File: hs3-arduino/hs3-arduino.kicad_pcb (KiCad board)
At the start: 2 copper layers, 68.6 x 53.3 mm, 30 parts, among them J1 Conn_01x02, J1 Serial, J2 USB_C_Receptacle_USB2.0, J4 LED Data, J5 I2C Header, J6 I2C Header, J7 I2C Header, J8 I2C Header, P1 Power, P2 Analog, P3 Digital, P4 Digital, P5 CONN_01X01, P6 CONN_01X01, P7 CONN_01X01, P8 CONN_01X01, SW1 Reset, SW2 Boot Option, U1 AMS1117-3.3, U2 ESP32-WROOM-32E, U3 TXB0102DCT

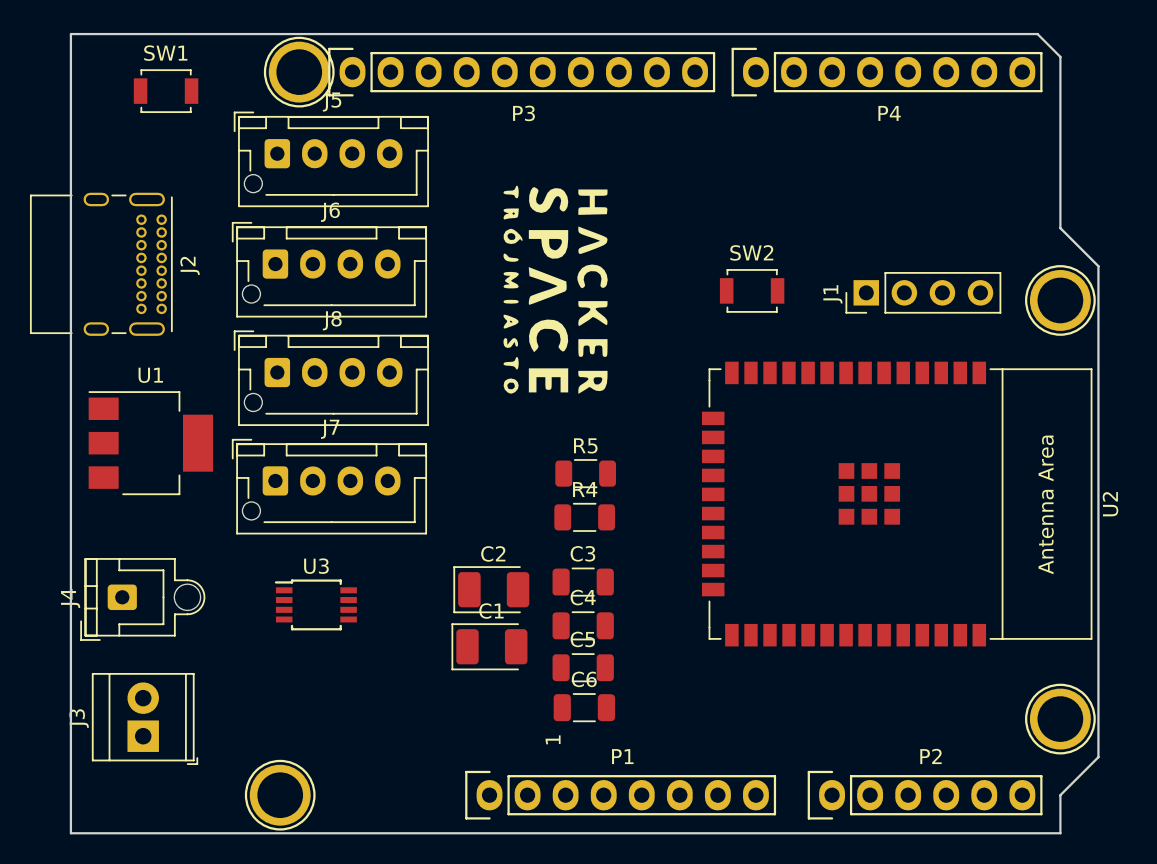
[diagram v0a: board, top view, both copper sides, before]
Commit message: Adding duplicated Arduino pins
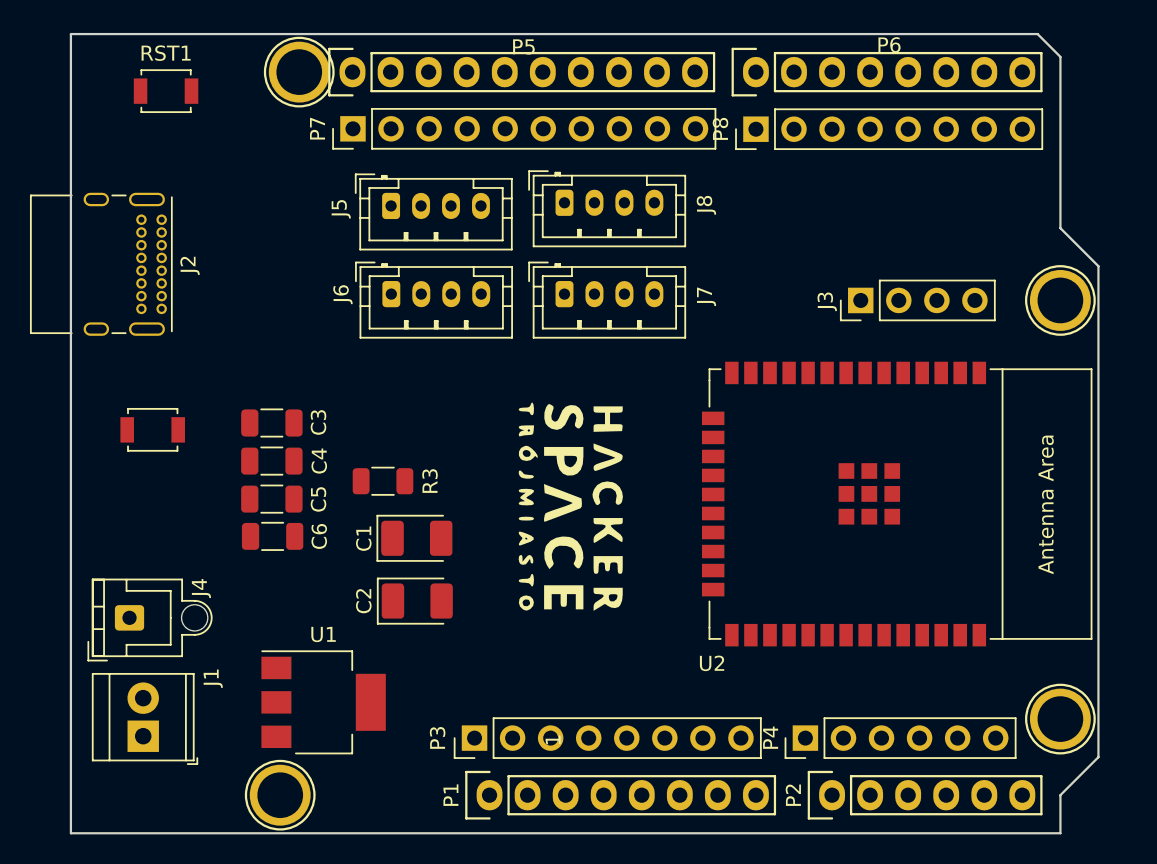
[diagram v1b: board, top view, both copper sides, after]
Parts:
- removed R5: 10k, Resistor_SMD:R_1206_3216Metric
- removed U3: TXB0102DCT, Package_SO:TSSOP-8_3x3mm_P0.65mm
- added P3: Power, Connector_PinHeader_2.54mm:PinHeader_1x08_P2.54mm_Vertical, F.Cu at (137.9, 120.0)
- added P4: Analog, Connector_PinHeader_2.54mm:PinHeader_1x06_P2.54mm_Vertical, F.Cu at (160.0, 120.0)
- added P7: Digital, Connector_PinHeader_2.54mm:PinHeader_1x10_P2.54mm_Vertical, F.Cu at (129.8, 79.3)
- added P8: Digital, Connector_PinHeader_2.54mm:PinHeader_1x08_P2.54mm_Vertical, F.Cu at (156.7, 79.4)
- J5, J6, J7, J8: footprint Connector_JST:JST_XH_B4B-XH-AM_1x04_P2.50mm_Vertical -> Connector_JST:JST_PH_B4B-PH-K_1x04_P2.00mm_Vertical
- moved BOOT1 41.1 mm to (116.5, 99.4)
- moved C6 23.7 mm to (124.5, 106.6)
- moved C5 23.6 mm to (124.4, 104.1)
- moved C4 23.5 mm to (124.4, 101.5)
- moved C3 23.3 mm to (124.4, 99.0)
- moved J7 23.0 mm to (143.9, 90.4)
- moved J8 22.3 mm to (143.9, 84.3)
- moved U1 20.8 mm to (127.9, 117.6)
- moved G*** 14.5 mm to (144.3, 104.6)
- moved R3 13.7 mm to (131.8, 102.9)
- moved C1 8.80 mm to (134.1, 106.7)
- moved J5 8.36 mm to (132.4, 84.5)
- moved J6 7.99 mm to (132.4, 90.4)
- moved C2 5.16 mm to (134.1, 110.9)
- moved J4 1.45 mm to (114.9, 112.0)
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- renumbered SW2 to BOOT1, J1 to J3, P6 to P10, P7 to P11, P8 to P12, P3 to P5, P4 to P6, P5 to P9, R4 to R3, SW1 to RST1
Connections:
- J4 pad 1: Net-(J4-Pad1) -> /LED Data
